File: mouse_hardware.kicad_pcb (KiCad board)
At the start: 2 copper layers, 8.9 x 15.9 mm, 44 parts, among them IC1 ADP150AUJZ-2.0-R7, IC2 AP2112K-3.3TRG1, J1 Conn_01x04_Pin, SW1 SW_Push, SW5 SW_Push, U1 STM32F103RETx, U2 PMW3360DM-T2QU, Y1 8MHz

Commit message: Start routing
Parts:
- added J2: Conn_01x04_Pin, Connector_PinHeader_2.54mm:PinHeader_1x04_P2.54mm_Horizontal, F.Cu at (23.9, 82.3)
- R3: value R -> 10K
- moved IC2 96.0 mm to (19.3, 48.2), turned to 180 degrees
- moved D2 94.3 mm to (14.7, 21.3), turned to 180 degrees
- moved SW5 93.8 mm to (18.7, 56.7), turned to 180 degrees
- moved R10 85.6 mm to (19.8, 21.3)
- moved C16 80.7 mm to (20.5, 65.2), turned to -90 degrees
- moved C12 79.7 mm to (14.7, 49.8), turned to 90 degrees
- moved U1 75.2 mm to (38.5, 79.5), turned to 180 degrees
- moved R7 72.6 mm to (17.0, 65.3), turned to 90 degrees
- moved R4 71.5 mm to (24.9, 32.0), turned to 180 degrees
- moved C13 71.4 mm to (24.9, 37.1)
- moved C19 70.8 mm to (28.4, 53.3), turned to 180 degrees
- moved C20 70.8 mm to (28.4, 56.9), turned to 180 degrees
- moved C11 70.6 mm to (23.9, 49.8), turned to 90 degrees
- moved C7 67.9 mm to (29.4, 81.5), turned to 90 degrees
- moved C17 64.2 mm to (49.7, 91.2), turned to 180 degrees
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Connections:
- U1 pad 5: unconnected-(U1-PD0-Pad5) -> OSC_IN
- U1 pad 6: unconnected-(U1-PD1-Pad6) -> OSC_OUT
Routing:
- net +5V: track 0.00 -> 101.1 mm
- net USBDP: track 0.00 -> 78.1 mm, vias 0 -> 4
- net USBDM: track 0.00 -> 77.8 mm, vias 0 -> 4
- net NRST: track 0.00 -> 43.4 mm, vias 0 -> 2
- net +3V3: track 0.00 -> 40.8 mm, vias 0 -> 2
- net SCK: track 0.00 -> 30.9 mm, vias 0 -> 4
- net MISO: track 0.00 -> 25.5 mm
- net MOSI: track 0.00 -> 21.0 mm
- net OSC_OUT: track 0.00 -> 19.3 mm
- net OSC_IN: track 0.00 -> 15.1 mm
- net LEFT_CLICK: track 0.00 -> 13.7 mm
- net MOTION: track 0.00 -> 13.4 mm
- net MIDDLE_CLICK: track 0.00 -> 12.9 mm
- net RIGHT_CLICK: track 0.00 -> 12.7 mm
- net Net-(U1-BOOT0): track 0.00 -> 9.90 mm
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- added copper zone on In1.Cu, net +3V3
- added copper zone on In2.Cu, net +3V3
- added copper zone on B.Cu, net GND
- added copper zone on F.Cu, net GND
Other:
- copper layers 2 -> 4

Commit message: Finish designing and routing pcb
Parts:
- added H1: MountingHole_Pad, Hole:Hole_1.8mm_1.2mm, F.Cu at (57.1, 25.4)
- added H2: MountingHole_Pad, Hole:Hole_1.8mm_1.2mm, F.Cu at (37.1, 25.4)
- added H3: MountingHole_Pad, Hole:Hole_1.8mm_1.2mm, F.Cu at (17.1, 25.4)
- J1, J2: footprint Connector_PinHeader_2.54mm:PinHeader_1x04_P2.54mm_Horizontal -> PinHeader:PinHeader_1x04_P2.54mm_Horizontal
- moved R2 4.49 mm to (35.2, 68.5)
- moved C1 0.62 mm to (46.8, 74.8)
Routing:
- net STATUS_LED: track 0.00 -> 108.2 mm, vias 0 -> 4
- net +3V3: track 40.8 -> 106.1 mm, vias 2 -> 26
- net +2V: track 3.40 -> 51.3 mm, vias 0 -> 2
- net NRST: track 43.4 -> 90.8 mm, vias 2 -> 6
- net MISO: track 25.5 -> 58.4 mm, vias 0 -> 4
- net NCS: track 0.00 -> 25.5 mm, vias 0 -> 2
- net MOSI: track 21.0 -> 42.4 mm, vias 0 -> 4
- net DPI_SWITCH: track 0.00 -> 12.8 mm
- net SCK: track 30.9 -> 25.1 mm, vias 4 -> 2
- net Net-(U1-PB2): track 0.00 -> 4.94 mm
- net USBDM: track 77.8 -> 78.8 mm
- net Net-(U2-LED_P): track 7.60 -> 8.16 mm
- net (no net): vias 3 -> 0
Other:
- board size 8.9 x 15.9 mm -> 51 x 82 mm

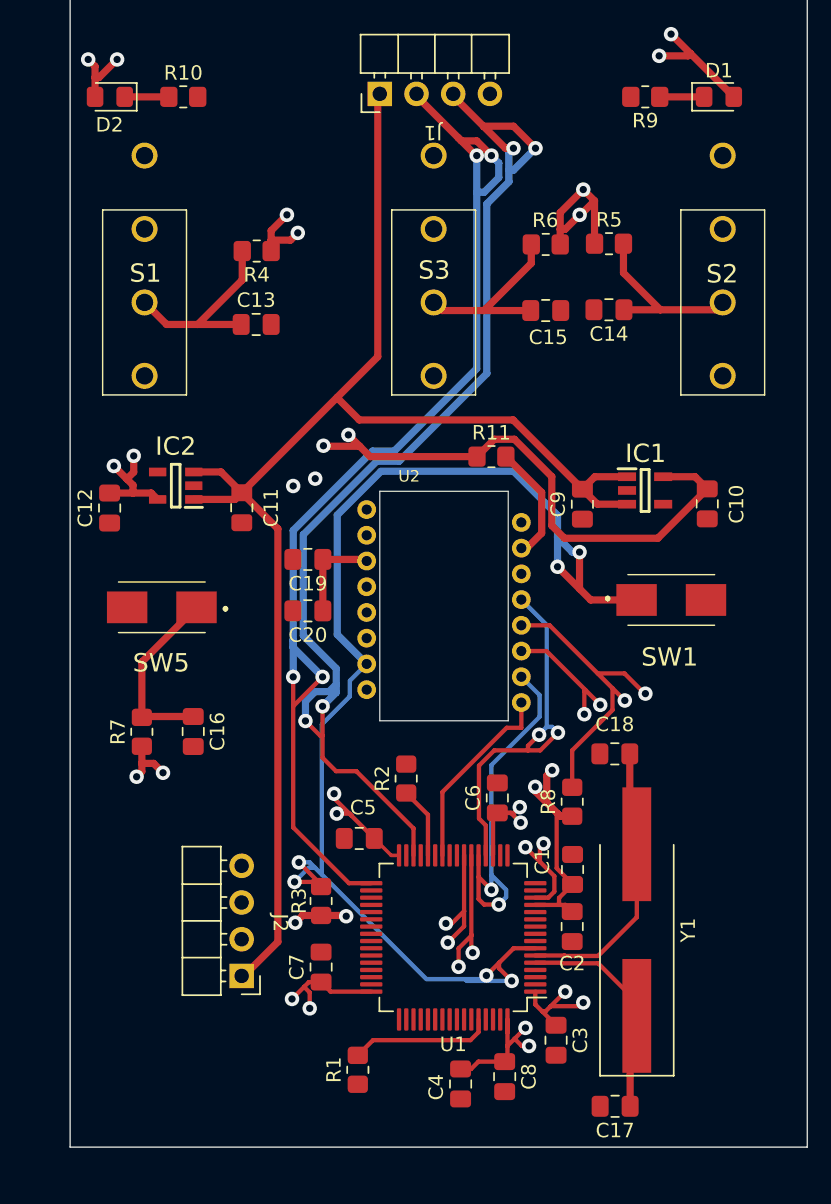
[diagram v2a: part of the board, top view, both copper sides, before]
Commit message: Connect SCLK and SWDIO
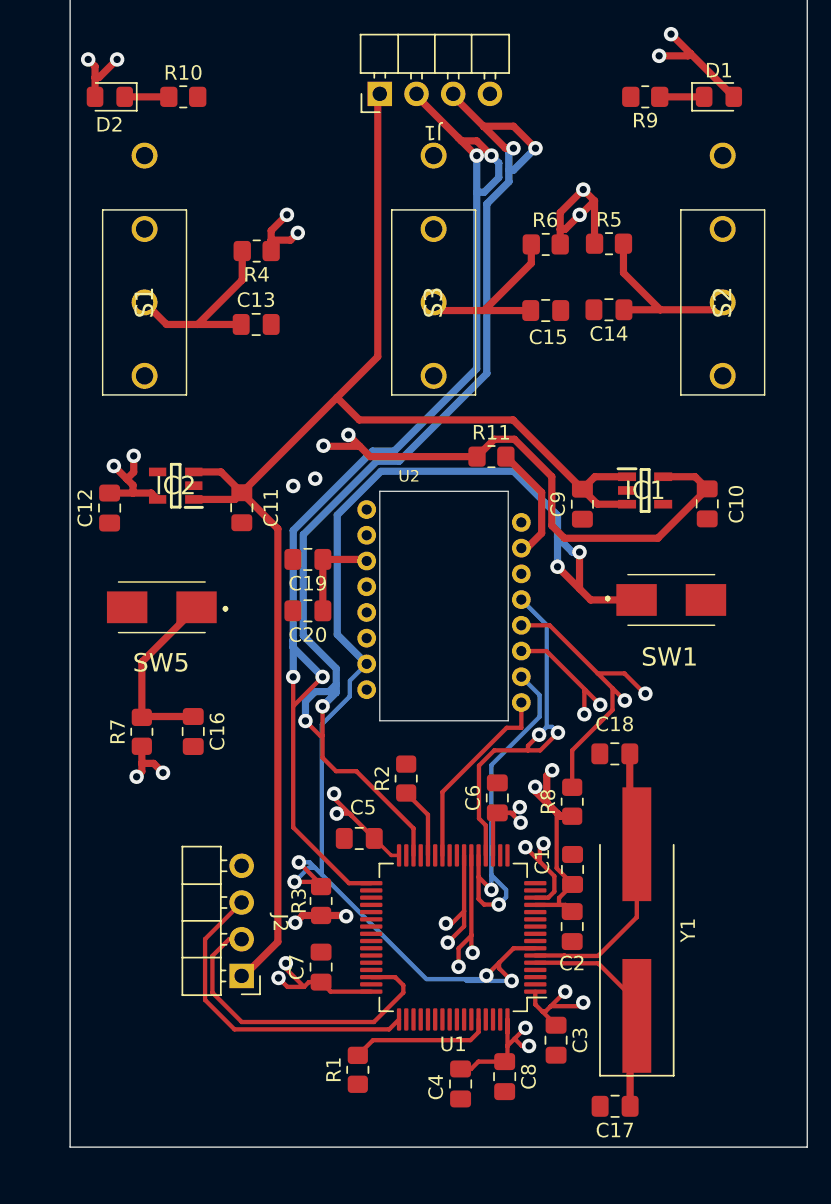
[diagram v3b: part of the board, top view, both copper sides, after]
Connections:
- U1 pad 46: unconnected-(U1-PA13-Pad46) -> SWDIO
- U1 pad 49: unconnected-(U1-PA14-Pad49) -> SWCLK
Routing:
- net SWDIO: track 0.00 -> 22.9 mm
- net SWCLK: track 0.00 -> 22.3 mm
- net +3V3: track 106.1 -> 107.5 mm
